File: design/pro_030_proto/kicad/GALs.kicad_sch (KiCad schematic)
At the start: 22 parts, among them IC10 ATF22V10C, IC14 ATF22V10C, IC2 ATF22V10C, IC22 ATF22V10C, IC3 ATF22V10C, IC4 ATF22V10C, IC5 ATF22V10C, IC6 ATF22V10C, IC7 ATF22V10C

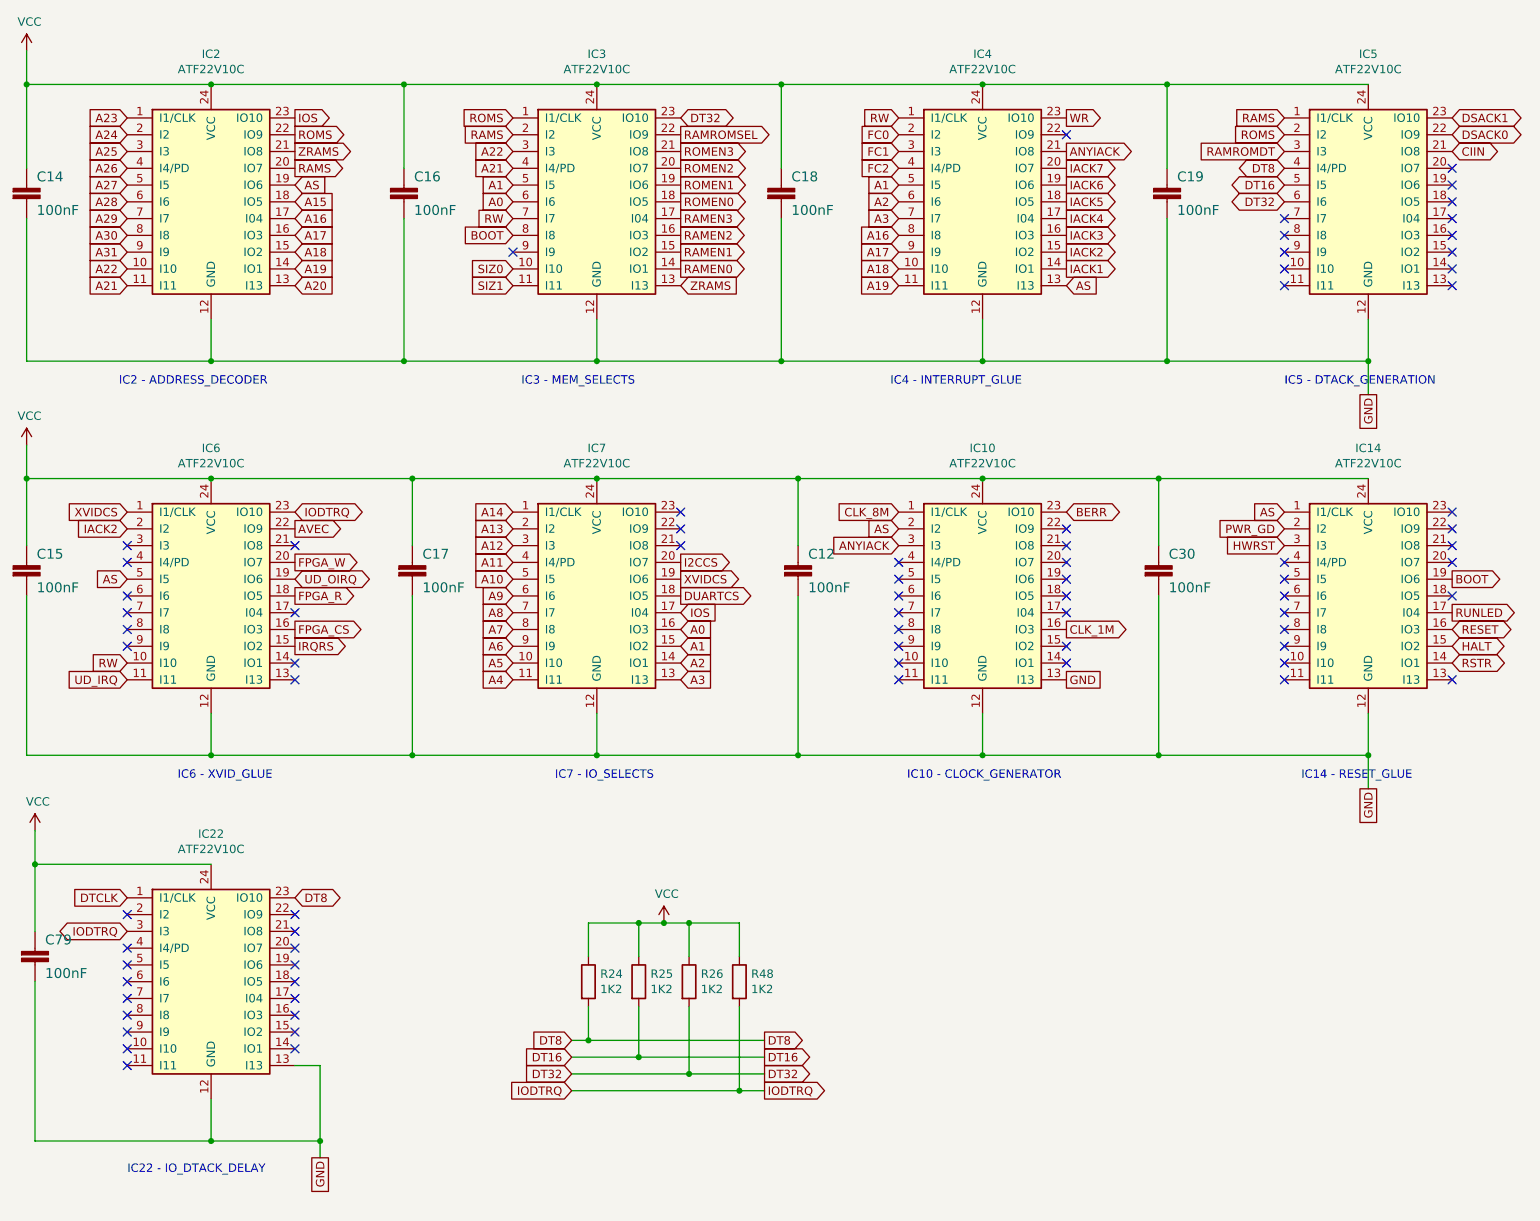
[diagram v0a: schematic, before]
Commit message: Surface DS in various GALS
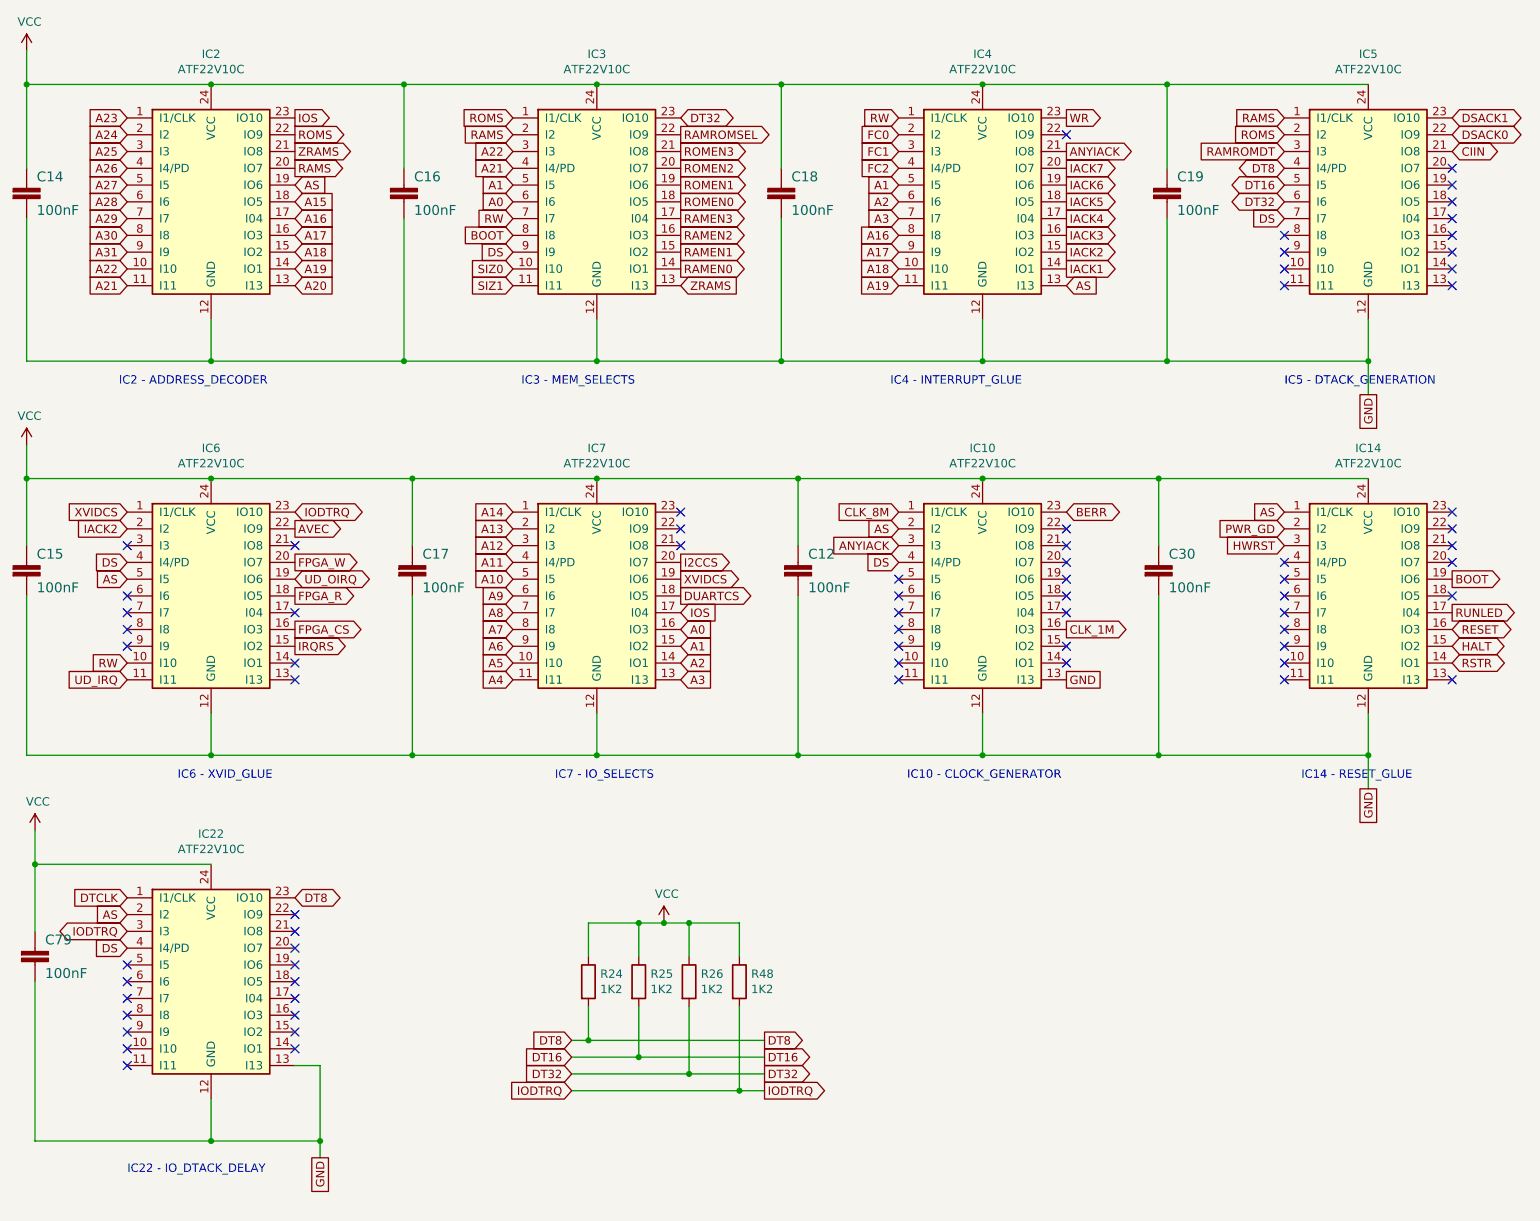
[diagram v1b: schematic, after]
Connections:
- net AS: now also IC22.2 (I2)
- net DS: now reaches IC3.9 (I9)
- net DS: now also IC10.4 (I4/PD), IC22.4 (I4/PD), IC5.7 (I7), IC6.4 (I4/PD)
- no-connect marks 76 -> 70
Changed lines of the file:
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@@
   (no_connect (at 190.5 104.14))
   (no_connect (at 165.1 109.22))
-  (no_connect (at 48.26 96.52))
   (no_connect (at 223.52 96.52))
   (no_connect (at 165.1 101.6))
   (no_connect (at 190.5 101.6))
-  (no_connect (at 223.52 44.45))
   (no_connect (at 73.66 152.4))
   (no_connect (at 48.26 93.98))
@@
   (no_connect (at 73.66 162.56))
   (no_connect (at 248.92 96.52))
-  (no_connect (at 48.26 154.94))
   (no_connect (at 132.08 93.98))
   (no_connect (at 190.5 109.22))
   (no_connect (at 165.1 106.68))
-  (no_connect (at 106.68 49.53))
   (no_connect (at 190.5 93.98))
   (no_connect (at 48.26 101.6))
   (no_connect (at 165.1 99.06))
   (no_connect (at 248.92 46.99))
-  (no_connect (at 48.26 149.86))
   (no_connect (at 190.5 31.75))
   (no_connect (at 248.92 41.91))
@@
   (no_connect (at 73.66 154.94))
   (no_connect (at 132.08 91.44))
-  (no_connect (at 165.1 96.52))
   (no_connect (at 73.66 93.98))
   (no_connect (at 132.08 88.9))
@@
     )
   )
+  (global_label "AS" (shape input) (at 48.26 149.86 180) (fields_autoplaced)
+    (effects (font (size 1.27 1.27)) (justify right))
+    (property "Intersheet References" "${INTERSHEET_REFS}" (id 0) (at 43.6377 149.7806 0)
+      (effects (font (size 1.27 1.27)) (justify right) hide)
+    )
+  )
+  (global_label "DS" (shape input) (at 165.1 96.52 180) (fields_autoplaced)
+    (effects (font (size 1.27 1.27)) (justify right))
+    (property "Intersheet References" "${INTERSHEET_REFS}" (id 0) (at 160.2963 96.4406 0)
+      (effects (font (size 1.27 1.27)) (justify right) hide)
+    )
+  )
   (global_label "A1" (shape input) (at 165.1 39.37 180) (fields_autoplaced)
     (effects (font (size 1.27 1.27)) (justify right))
@@
     (property "Intersheet References" "${INTERSHEET_REFS}" (id 0) (at 0 0 0)
       (effects (font (size 1.27 1.27)) hide)
+    )
+  )
+  (global_label "DS" (shape input) (at 48.26 154.94 180) (fields_autoplaced)
+    (effects (font (size 1.27 1.27)) (justify right))
+    (property "Intersheet References" "${INTERSHEET_REFS}" (id 0) (at 43.4563 154.8606 0)
+      (effects (font (size 1.27 1.27)) (justify right) hide)
     )
   )
@@
     )
   )
+  (global_label "DS" (shape input) (at 48.26 96.52 180) (fields_autoplaced)
+    (effects (font (size 1.27 1.27)) (justify right))
+    (property "Intersheet References" "${INTERSHEET_REFS}" (id 0) (at 43.4563 96.4406 0)
+      (effects (font (size 1.27 1.27)) (justify right) hide)
+    )
+  )
   (global_label "RAMEN0" (shape output) (at 132.08 52.07 0) (fields_autoplaced)
     (effects (font (size 1.27 1.27)) (justify left))
@@
     )
   )
+  (global_label "DS" (shape input) (at 223.52 44.45 180) (fields_autoplaced)
+    (effects (font (size 1.27 1.27)) (justify right))
+    (property "Intersheet References" "${INTERSHEET_REFS}" (id 0) (at 218.7163 44.3706 0)
+      (effects (font (size 1.27 1.27)) (justify right) hide)
+    )
+  )
   (global_label "A28" (shape input) (at 48.26 41.91 180) (fields_autoplaced)
     (effects (font (size 1.27 1.27)) (justify right))
@@
     )
   )
+  (global_label "DS" (shape input) (at 106.68 49.53 180) (fields_autoplaced)
+    (effects (font (size 1.27 1.27)) (justify right))
+    (property "Intersheet References" "${INTERSHEET_REFS}" (id 0) (at 101.8763 49.4506 0)
+      (effects (font (size 1.27 1.27)) (justify right) hide)
+    )
+  )

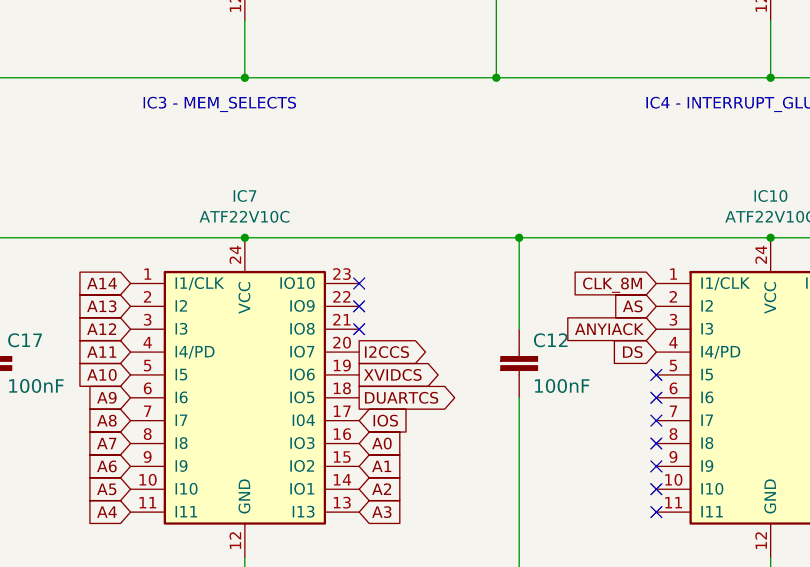
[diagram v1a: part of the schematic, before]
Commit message: Merge IDE decoder with main IO select on IC7
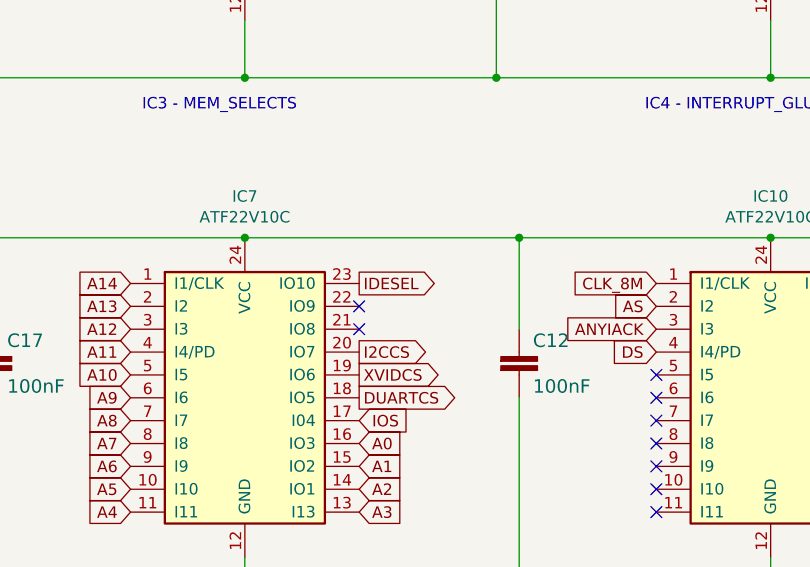
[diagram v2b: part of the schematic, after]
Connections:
- net IDESEL: now reaches IC7.23 (IO10)
- no-connect marks 70 -> 69
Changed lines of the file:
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@@
   (no_connect (at 73.66 162.56))
   (no_connect (at 248.92 96.52))
-  (no_connect (at 132.08 93.98))
   (no_connect (at 190.5 109.22))
   (no_connect (at 165.1 106.68))
@@
   (no_connect (at 132.08 91.44))
   (no_connect (at 73.66 93.98))
-  (no_connect (at 132.08 88.9))
+  (no_connect (at 132.08 93.98))
   (no_connect (at 73.66 157.48))
   (no_connect (at 190.5 91.44))
@@
     )
   )
+  (global_label "IDESEL" (shape output) (at 132.08 88.9 0) (fields_autoplaced)
+    (effects (font (size 1.27 1.27)) (justify left))
+    (property "Intersheet References" "${INTERSHEET_REFS}" (id 0) (at 140.8147 88.8206 0)
+      (effects (font (size 1.27 1.27)) (justify left) hide)
+    )
+  )
